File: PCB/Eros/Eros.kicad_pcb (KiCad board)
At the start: 4 copper layers, 65 x 71 mm, 114 parts, among them IC1 ADS1292RIPBS, J1 USB_C_PowerOnly_6P, J2 UART, J3 Li-ion, J4 Conn_01x08_Socket, J5 AudioJack3, J6 Micro_SD_Card, J7 Conn_01x03_Socket, Q1 BC817, SW1 SW_Push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

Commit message: add logos
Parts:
- added G***: LOGO, LOGO, B.Cu at (174.5, 53.8)
- added G***: LOGO, LOGO, B.Cu at (164.0, 106.2)
- moved G1 73.9 mm to (205.7, 113.7)

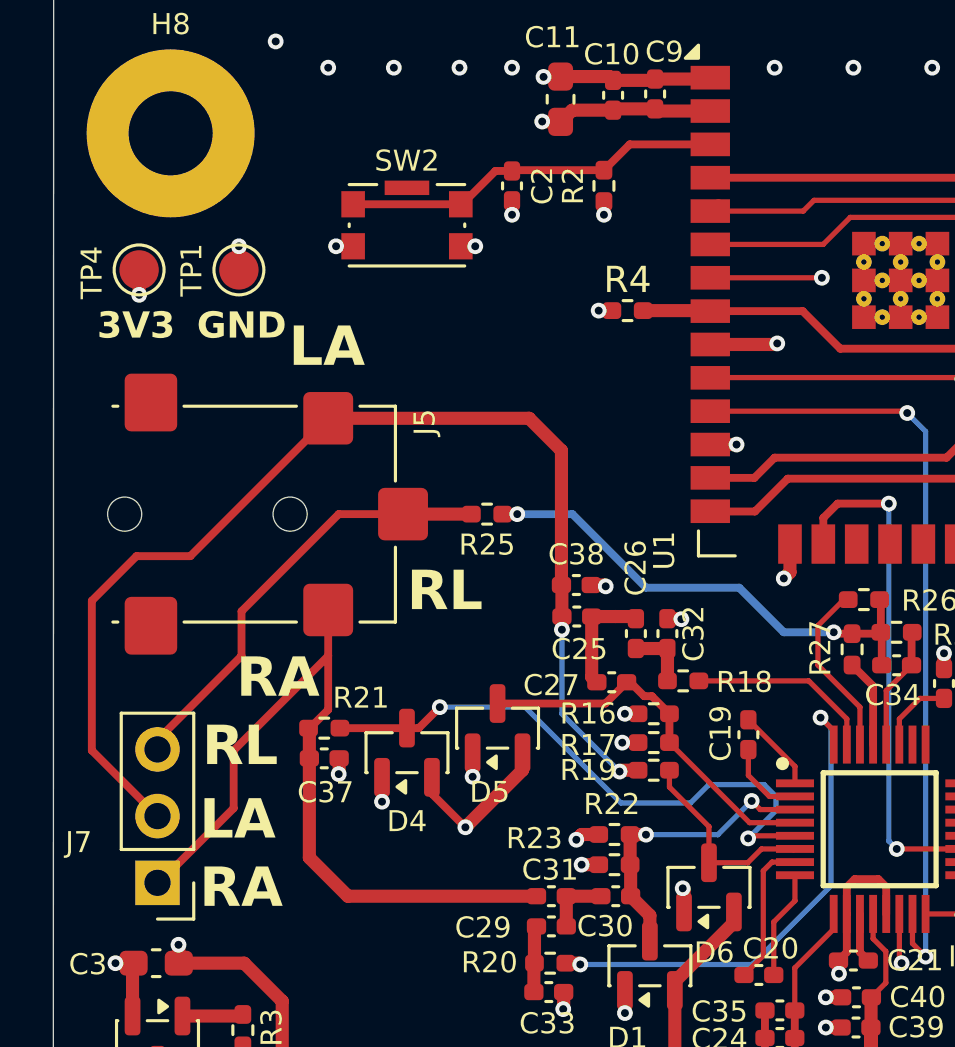
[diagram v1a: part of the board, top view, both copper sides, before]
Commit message: Remove sharp edges
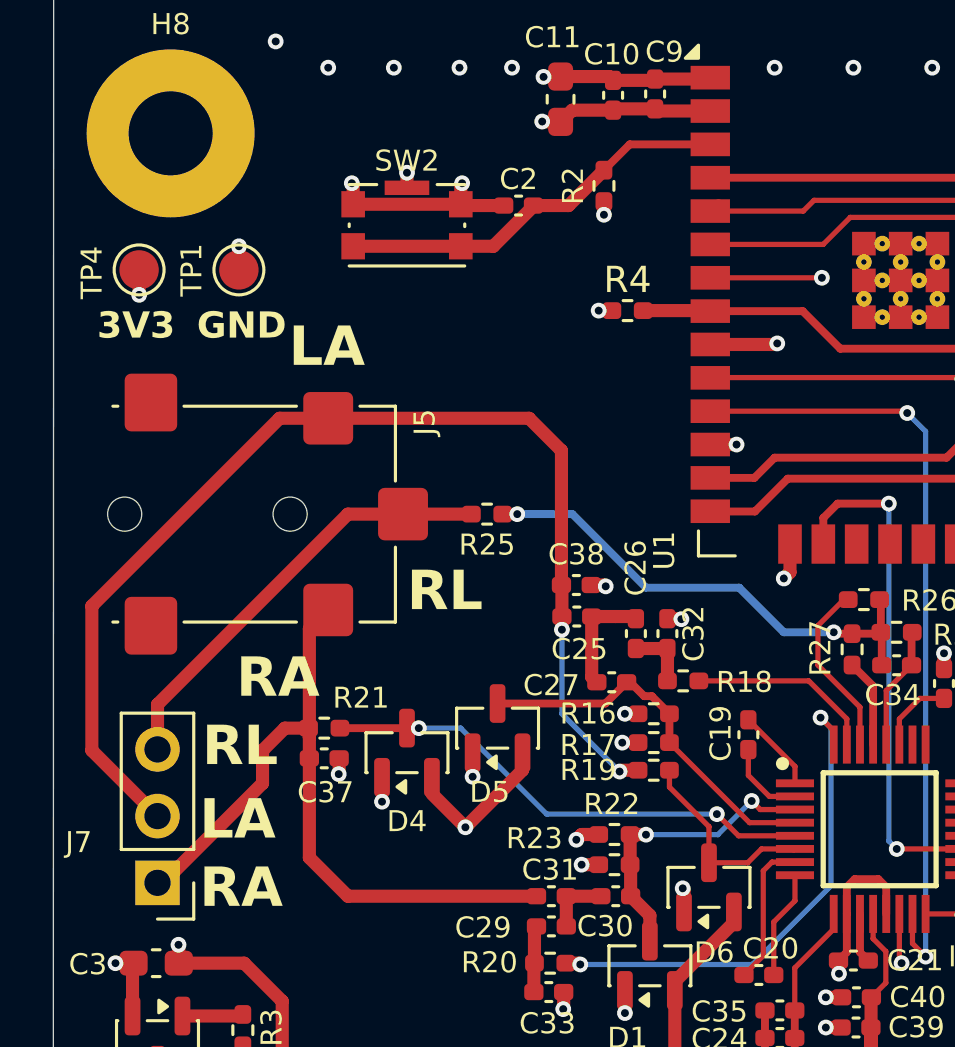
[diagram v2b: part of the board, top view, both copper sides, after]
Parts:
- moved C2 0.79 mm to (170.2, 63.2), turned to 180 degrees
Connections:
- SW2 pad 1: RESET -> GND
- SW2 pad 2: GND -> RESET
- SW2 pad SH: unconnected-(SW2-PadSH) -> GND
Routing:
- net GND: track 84.7 -> 91.0 mm
- net IN2N: track 22.8 -> 19.0 mm
- net RA: track 30.5 -> 28.4 mm
- net RESET: track 14.5 -> 15.2 mm
- added copper zone on In2.Cu, net GND

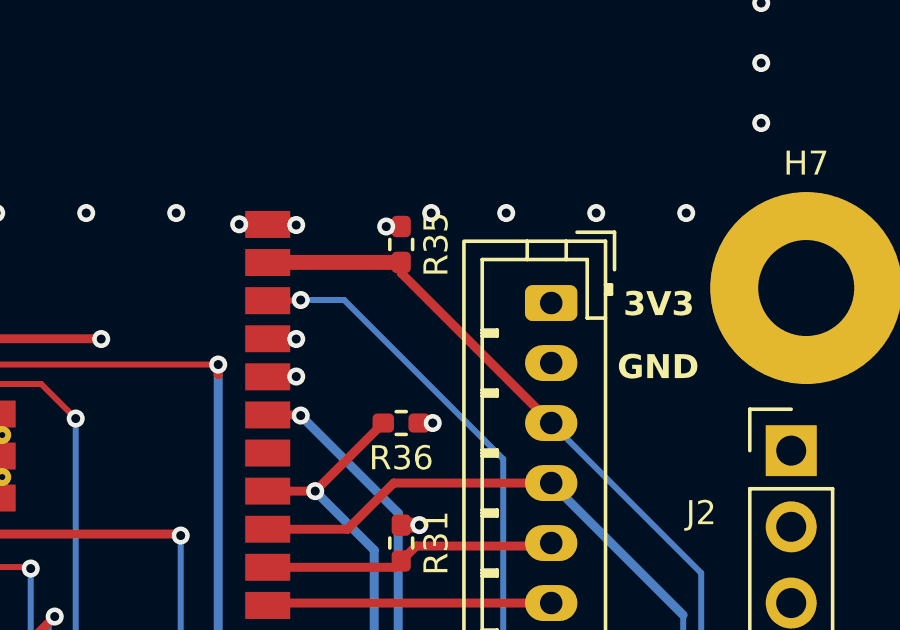
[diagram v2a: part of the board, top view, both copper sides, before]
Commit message: Add gnd pour around antenna
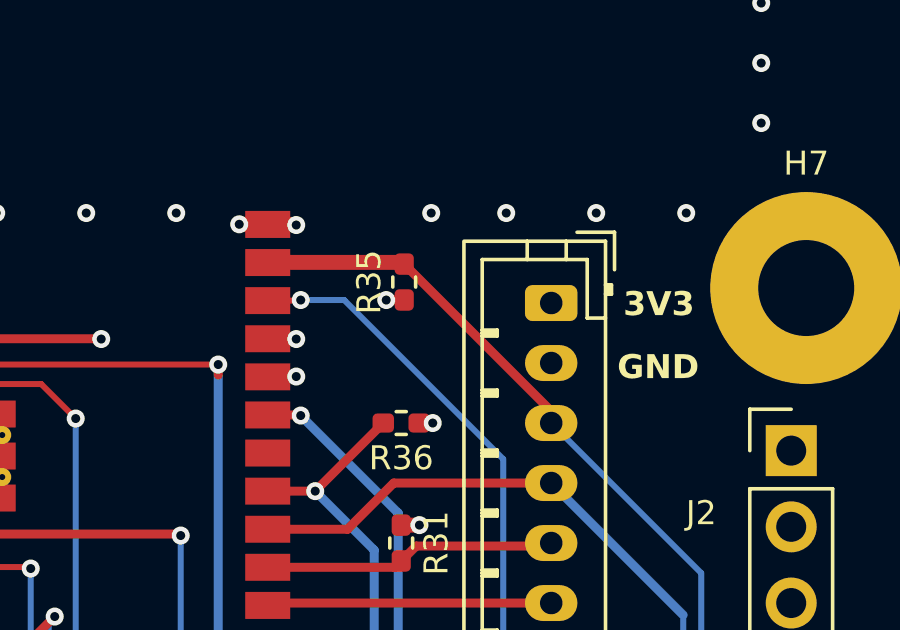
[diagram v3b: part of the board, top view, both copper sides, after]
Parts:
- moved R35 1.26 mm to (199.6, 60.3), turned to 90 degrees
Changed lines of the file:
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@@
 	(footprint "Resistor_SMD:R_0402_1005Metric_Pad0.72x0.64mm_HandSolder"
 		(layer "F.Cu")
-		(at 199.5 59.0475 -90)
+		(at 199.6 60.3 90)
 		(descr "Resistor SMD 0402 (1005 Metric), square (rectangular) end terminal, IPC-7351 nominal with elongated pad for handsoldering. (Body size source: IPC-SM-782 page 72, https://www.pcb-3d.com/wordpress/wp-content/uploads/ipc-sm-782a_amendment_1_and_2.pdf), generated with kicad-footprint-generator")
 		(tags "resistor handsolder")
@@
 		(attr smd)
 		(fp_line
-			(start -0.167621 0.38)
-			(end 0.167621 0.38)
+			(start -0.167621 -0.380001)
+			(end 0.167621 -0.380001)
 			(stroke
 				(width 0.12)
@@
 		)
 		(fp_line
-			(start -0.167621 -0.38)
-			(end 0.167621 -0.38)
+			(start -0.167621 0.380001)
+			(end 0.167621 0.380001)
 			(stroke
 				(width 0.12)
@@
 			(layer "F.SilkS")
 		)
-		(fp_rect
-			(start -1.11 -0.47)
-			(end 1.11 0.47)
+		(fp_poly
+			(pts
+				(xy -1.11 -0.47) (xy -1.11 0.47) (xy 1.11 0.47) (xy 1.11 -0.47)
+			)
 			(stroke
 				(width 0.05)
@@
 			(layer "F.CrtYd")
 		)
-		(fp_rect
-			(start -0.525 -0.27)
-			(end 0.525 0.27)
+		(fp_poly
+			(pts
+				(xy -0.525 -0.27) (xy -0.525 0.27) (xy 0.525 0.27) (xy 0.525 -0.27)
+			)
 			(stroke
 				(width 0.1)
@@
 		)
 		(pad "1" smd roundrect
-			(at -0.5975 0 270)
+			(at -0.5975 0 90)
 			(size 0.715 0.64)
 			(layers "F.Cu" "F.Mask" "F.Paste")
@@
 		)
 		(pad "2" smd roundrect
-			(at 0.5975 0 270)
+			(at 0.5975 0 90)
 			(size 0.715 0.64)
 			(layers "F.Cu" "F.Mask" "F.Paste")
@@
 	)
 	(segment
-		(start 199.5 58.45)
-		(end 199 58.45)
-		(width 0.5)
-		(layer "F.Cu")
-		(net 2)
-	)
-	(segment
 		(start 173.5 63.0975)
 		(end 173.5 63.6)
@@
 	)
 	(segment
+		(start 199.0025 60.8975)
+		(end 199 60.9)
+		(width 0.3)
+		(layer "F.Cu")
+		(net 2)
+	)
+	(segment
+		(start 199.6 60.8975)
+		(end 199.0025 60.8975)
+		(width 0.3)
+		(layer "F.Cu")
+		(net 2)
+	)
+	(segment
 		(start 193.7375 110.8625)
 		(end 193.75 110.85)
@@
 	)
 	(via
+		(at 199 60.9)
+		(size 0.6)
+		(drill 0.3)
+		(layers "F.Cu" "B.Cu")
+		(net 2)
+	)
+	(via
 		(at 193.75 110.85)
 		(size 0.6)
@@
 	)
 	(via
-		(at 199 58.45)
-		(size 0.6)
-		(drill 0.3)
-		(layers "F.Cu" "B.Cu")
-		(net 2)
-	)
-	(via
 		(at 200.55 65)
 		(size 0.6)
@@
 	)
 	(segment
+		(start 204.5 64.6025)
+		(end 204.5 65)
+		(width 0.3)
+		(layer "F.Cu")
+		(net 37)
+	)
+	(segment
 		(start 208.895 105.005)
 		(end 207.9 105.005)
@@
 	)
 	(segment
-		(start 199.5 59.645)
-		(end 199.5 60)
+		(start 199.6 59.7025)
+		(end 204.5 64.6025)
 		(width 0.3)
 		(layer "F.Cu")
@@
 	)
 	(segment
-		(start 199.5 60)
-		(end 204.5 65)
-		(width 0.3)
-		(layer "F.Cu")
-		(net 37)
-	)
-	(segment
 		(start 195.055 59.645)
 		(end 195.05 59.65)
@@
 		(hatch edge 0.5)
 		(priority 1)
-		(connect_pads
+		(connect_pads yes
 			(clearance 0.5)
 		)
@@
 		(polygon
 			(pts
-				(xy 210.6 49) (xy 218 49) (xy 218 59) (xy 152 59) (xy 152 49) (xy 162 49) (xy 162 57.4) (xy 210.3 57.08)
+				(xy 210.6 49) (xy 218 49) (xy 218 59) (xy 152 59) (xy 152 49) (xy 162 49) (xy 162 57.4) (xy 210.6 57.4)
 			)
 		)
@@
 		(layer "In2.Cu")
 		(hatch edge 0.5)
-		(priority 2)
 		(connect_pads
 			(clearance 0.5)

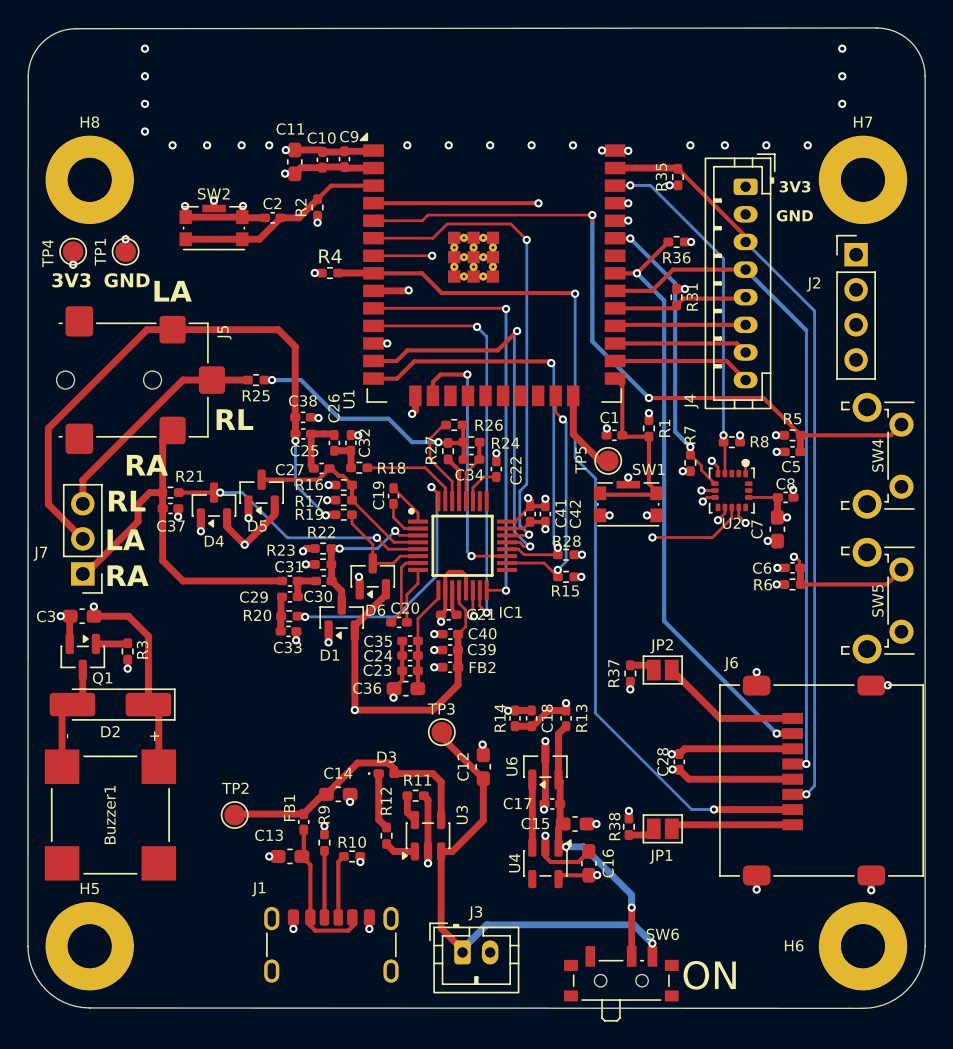
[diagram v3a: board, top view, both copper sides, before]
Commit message: Add separate AGND
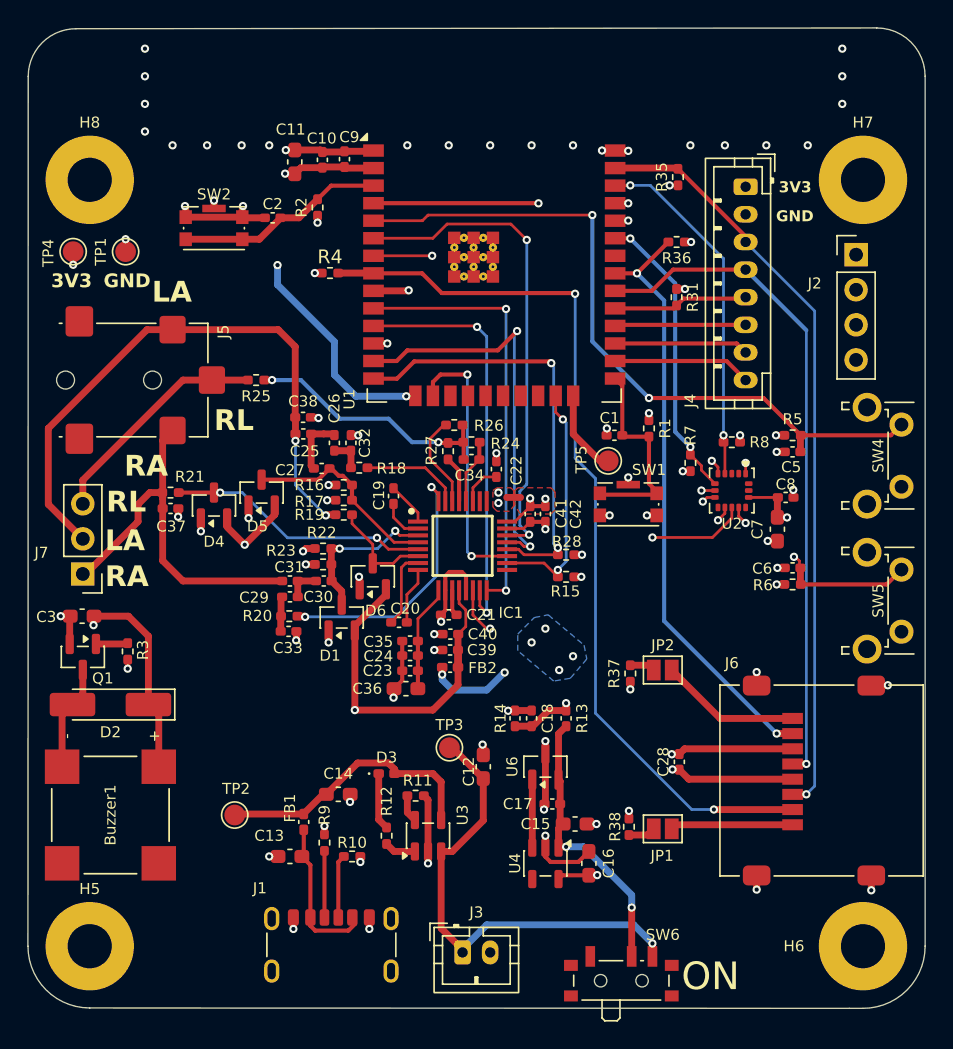
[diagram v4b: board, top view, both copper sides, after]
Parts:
- added NT1: NetTie_2, NetTie:NetTie-2_SMD_Pad0.5mm, F.Cu at (187.7, 83.5)
- moved TP3 1.25 mm to (183.1, 101.6)
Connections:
- C21 pad 2: GND -> GND_A
- C22 pad 2: GND -> GND_A
- C23 pad 2: GND -> GND_A
- C24 pad 2: GND -> GND_A
- C32 pad 2: GND -> GND_A
- C33 pad 2: GND -> GND_A
- C35 pad 2: GND -> GND_A
- C36 pad 2: GND -> GND_A
- C37 pad 1: GND -> GND_A
- C38 pad 2: GND -> GND_A
- C39 pad 2: GND -> GND_A
- C40 pad 2: GND -> GND_A
- D1 pad 1: GND -> GND_A
- D4 pad 1: GND -> GND_A
- D5 pad 1: GND -> GND_A
- D6 pad 1: GND -> GND_A
- IC1 pad 10: GND -> GND_A
- IC1 pad 13: GND -> GND_A
- R17 pad 1: GND -> GND_A
- R22 pad 1: GND -> GND_A
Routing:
- net GND_A: track 0.00 -> 19.9 mm, vias 0 -> 17
- net +3.3V: track 53.5 -> 60.7 mm, vias 24 -> 29
- net GND: track 91.0 -> 85.6 mm, vias 77 -> 63
- net Acc: track 35.8 -> 34.6 mm
- net BUTTON_2: track 52.7 -> 51.9 mm
- net Net-(IC1-PGA2P): track 4.71 -> 4.13 mm
- added copper zone on B.Cu, net +3.3V
- added copper zone on F.Cu, net GND
- added copper zone on F.Cu, net GND_A
- added copper zone on In1.Cu, net GND_A
- added copper zone on In2.Cu, net GND_A

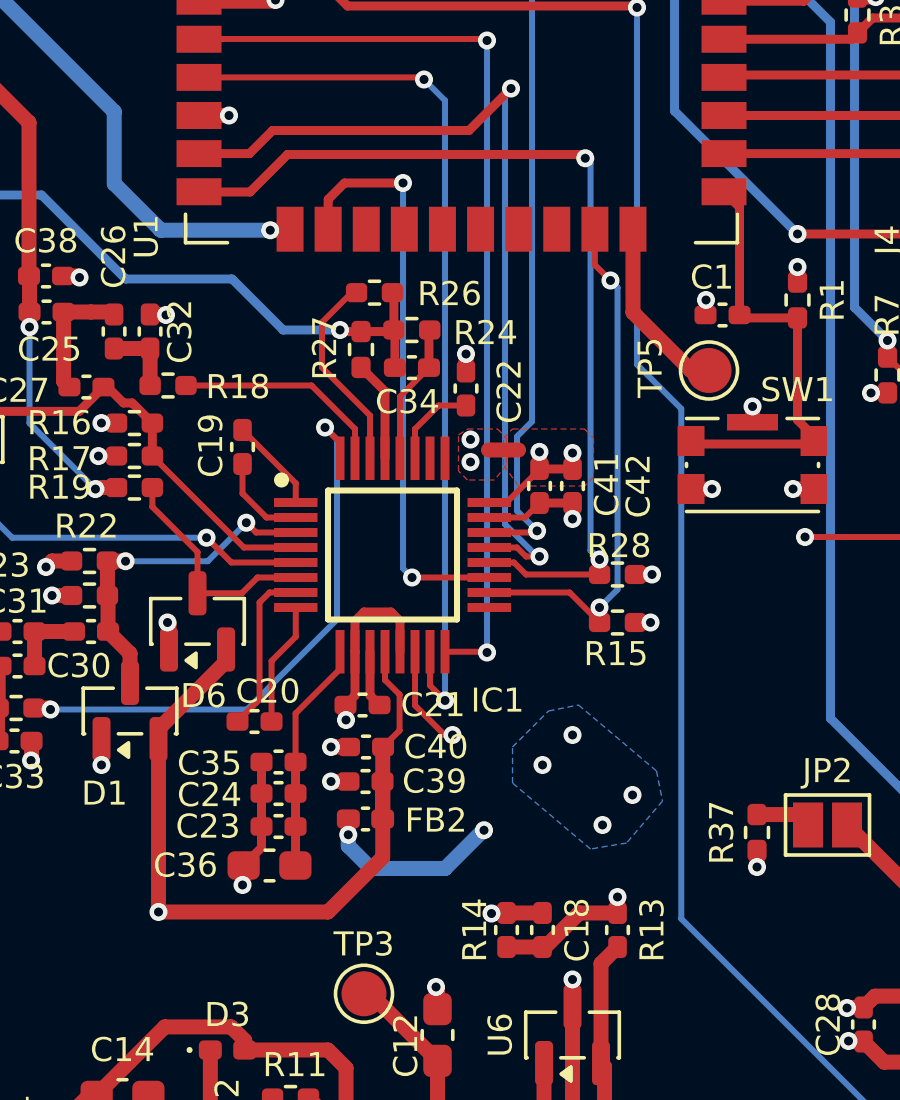
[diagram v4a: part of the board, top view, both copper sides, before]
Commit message: Connect GND and GND_A according to datasheet
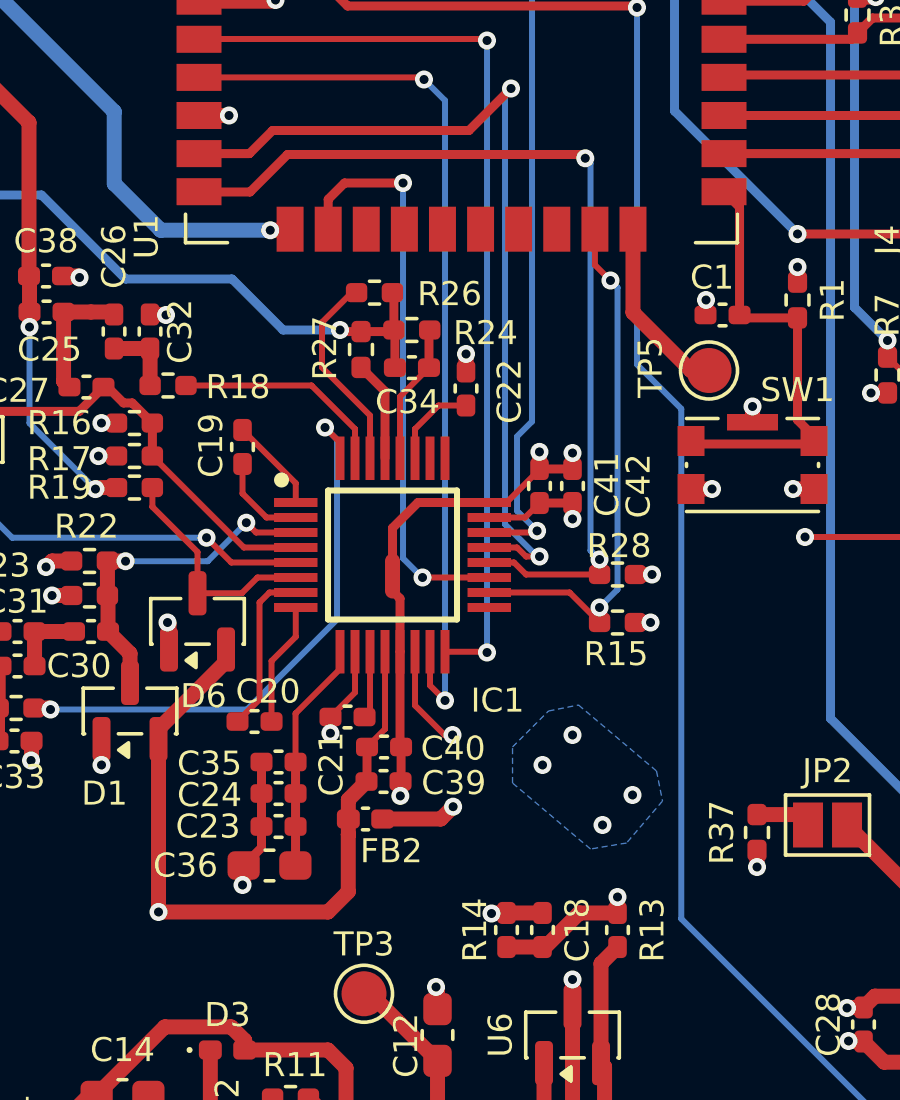
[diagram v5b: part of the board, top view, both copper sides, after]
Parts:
- moved G*** 59.9 mm to (193.2, 54.0)
- moved NT1 5.60 mm to (184.0, 87.7), turned to 90 degrees
- moved G*** 4.13 mm to (170.4, 54.0)
- moved C21 0.64 mm to (182.5, 92.4)
- moved C39 0.60 mm to (183.7, 94.5), turned to 0 degrees
- moved C40 0.60 mm to (183.7, 93.4), turned to 0 degrees
- turned FB2 to 0 degrees
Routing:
- net GND: track 85.6 -> 90.3 mm
- net +3.3V: track 60.7 -> 57.0 mm, vias 29 -> 28
- net GND_A: track 19.9 -> 22.5 mm, vias 17 -> 14
- net AVDD: track 67.8 -> 66.1 mm
- net BUZZER: track 68.6 -> 69.5 mm
- removed copper zone on F.Cu, net GND
- removed copper zone on F.Cu, net GND_A
